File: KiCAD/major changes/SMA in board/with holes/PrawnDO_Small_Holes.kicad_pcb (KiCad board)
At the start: 2 copper layers, 113 x 86.8 mm, 81 parts, among them IC1 74LVT245D,118, IC2 74LVT245D,118, IC3 74LVT245D,118, IC4 74LVT245D,118, J1 do15, J10 do6, J11 do5, J12 do4, J13 do3, J14 do2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

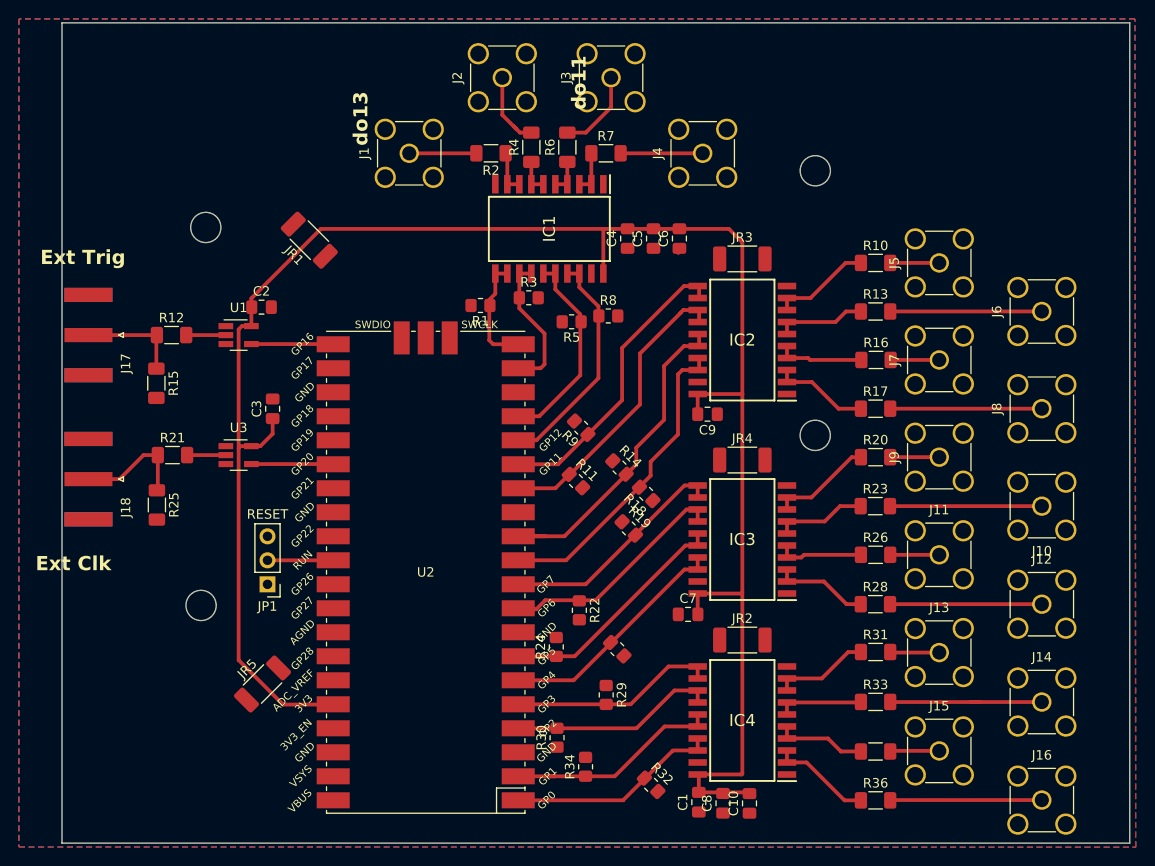
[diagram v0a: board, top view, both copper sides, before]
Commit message: Added Mounting holes to board
Mounting holes line up with Prawnblaster.

Changed layout of components to make spacing better
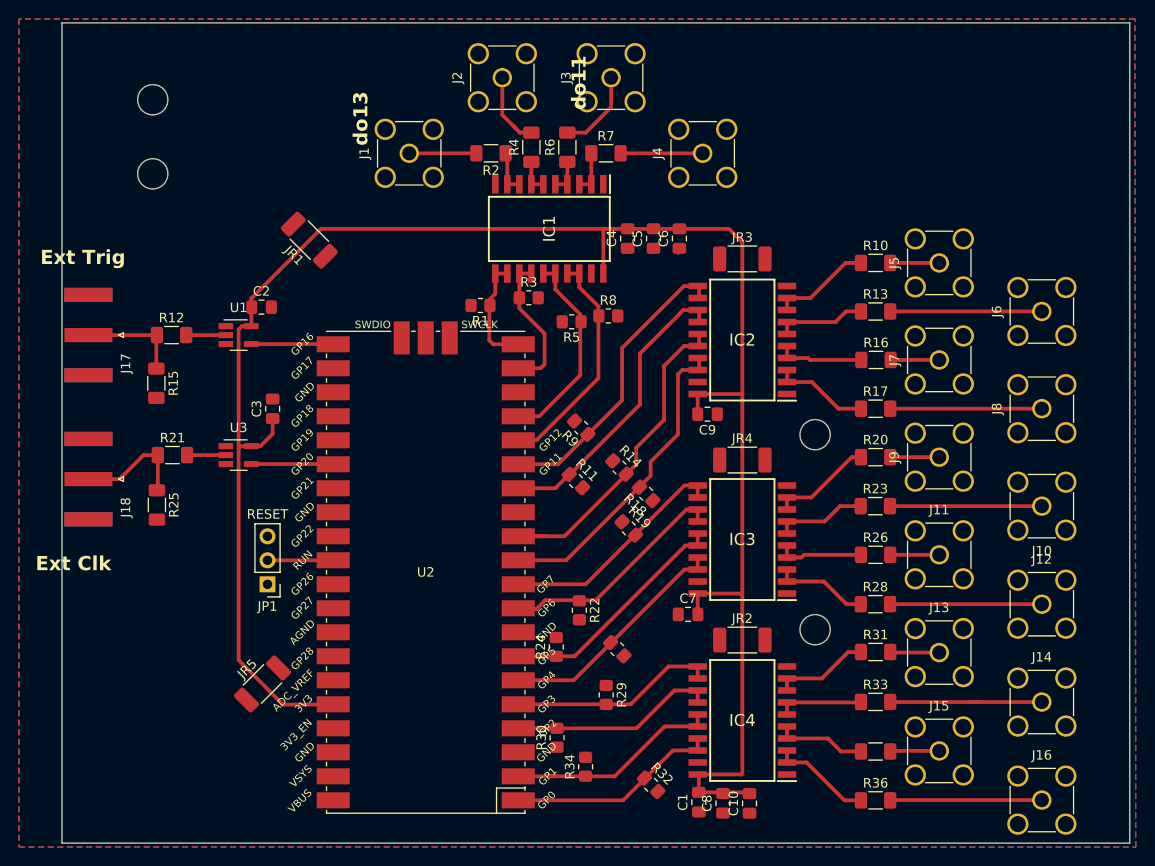
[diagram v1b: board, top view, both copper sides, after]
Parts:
- moved REF** 53.8 mm to (81.5, 62.4)
- moved REF** 27.9 mm to (151.6, 97.8)
- moved REF** 20.6 mm to (151.6, 118.4)
- moved REF** 7.98 mm to (81.5, 70.2)
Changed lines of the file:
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@@
   )
   (footprint "MountingHole:MountingHole_3.2mm_M3_ISO7380" (layer "F.Cu")
-    (at 87.12 75.871)
+    (at 81.509 70.195)
     (descr "Mounting Hole 3.2mm, no annular, M3, ISO7380")
     (tags "mounting hole 3.2mm no annular m3 iso7380")
@@
   )
   (footprint "MountingHole:MountingHole_3.2mm_M3_ISO7380" (layer "F.Cu")
-    (at 151.62 97.871)
+    (at 151.609 118.439)
     (descr "Mounting Hole 3.2mm, no annular, M3, ISO7380")
     (tags "mounting hole 3.2mm no annular m3 iso7380")
@@
   )
   (footprint "MountingHole:MountingHole_3.2mm_M3_ISO7380" (layer "F.Cu")
-    (at 86.62 115.871)
+    (at 81.509 62.354)
     (descr "Mounting Hole 3.2mm, no annular, M3, ISO7380")
     (tags "mounting hole 3.2mm no annular m3 iso7380")
@@
   )
   (footprint "MountingHole:MountingHole_3.2mm_M3_ISO7380" (layer "F.Cu")
-    (at 151.62 69.871)
+    (at 151.6 97.8)
     (descr "Mounting Hole 3.2mm, no annular, M3, ISO7380")
     (tags "mounting hole 3.2mm no annular m3 iso7380")
